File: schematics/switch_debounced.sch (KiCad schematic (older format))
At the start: 6 parts, among them SW1 SW_SPST

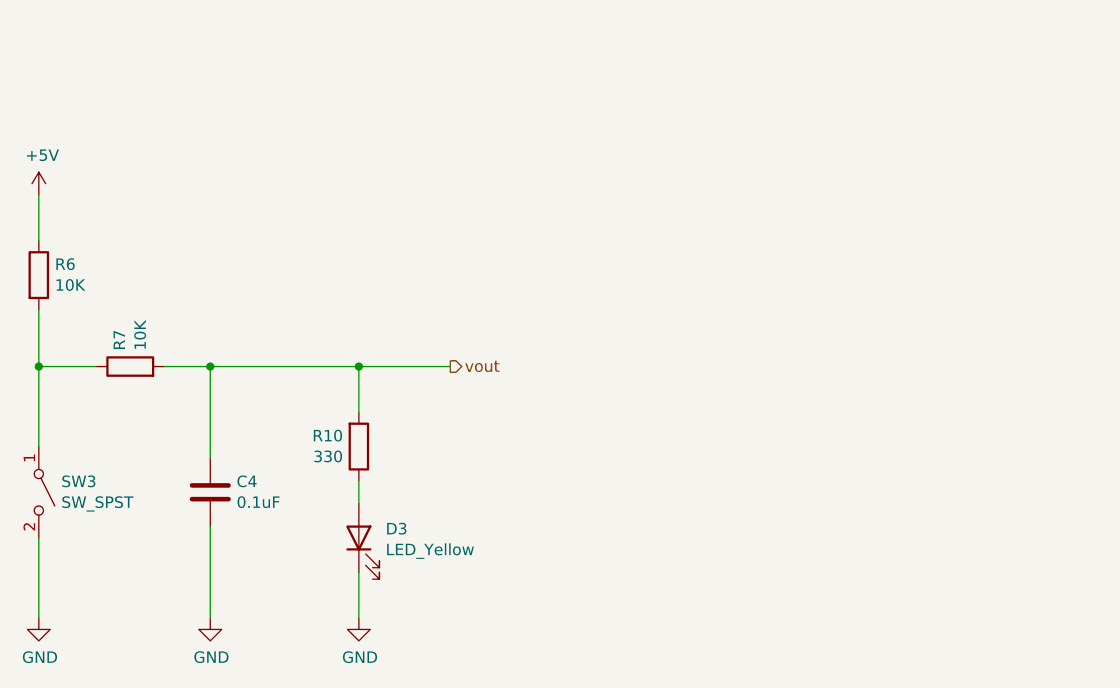
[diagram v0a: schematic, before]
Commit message: fixed lcd pin connections and xtra halls
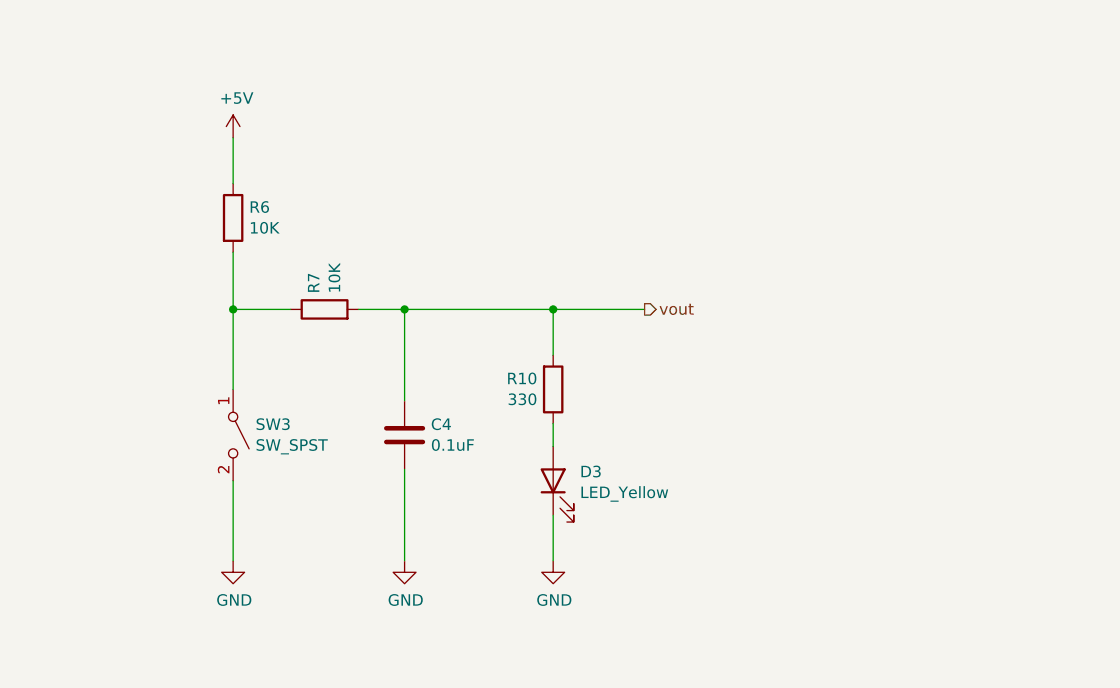
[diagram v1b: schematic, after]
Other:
- moved on the sheet: C4, D3, R10, R6, R7, SW3
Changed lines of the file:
@@
 EESchema Schematic File Version 4
-LIBS:odometer_project-cache
 EELAYER 30 0
 EELAYER END
 $Descr A4 11693 8268
 encoding utf-8
-Sheet 4 4
-Title ""
-Date ""
-Rev ""
-Comp ""
+Sheet 2 4
+Title "Odometer I2C Interface"
+Date "2020-10-03"
+Rev "2"
+Comp "DES Gang"
 Comment1 ""
 Comment2 ""
@@
 L Switch:SW_SPST SW1
 U 1 1 5F7A2F6B
-P 4050 4500
+P 4900 4250
 AR Path="/5F7B6E63/5F7A2F6B" Ref="SW1"  Part="1"
 AR Path="/5F7BFBA0/5F7A2F6B" Ref="SW2"  Part="1"
@@
 AR Path="/5F7CC063/5F7A2F6B" Ref="SW2"  Part="1"
 AR Path="/5F7CF7BD/5F7A2F6B" Ref="SW3"  Part="1"
-F 0 "SW3" V 4004 4598 50  0000 L CNN
-F 1 "SW_SPST" V 4095 4598 50  0000 L CNN
-F 2 "Button_Switch_THT:SW_PUSH_6mm_H4.3mm" H 4050 4500 50  0001 C CNN
-F 3 "~" H 4050 4500 50  0001 C CNN
-	1    4050 4500
+F 0 "SW3" V 4854 4348 50  0000 L CNN
+F 1 "SW_SPST" V 4945 4348 50  0000 L CNN
+F 2 "Button_Switch_THT:SW_PUSH_6mm_H4.3mm" H 4900 4250 50  0001 C CNN
+F 3 "~" H 4900 4250 50  0001 C CNN
+	1    4900 4250
 	0    1    1    0
 $EndComp
@@
 L power:GND #PWR0101
 U 1 1 5F7A3360
-P 4050 5050
+P 4900 4800
 AR Path="/5F7B6E63/5F7A3360" Ref="#PWR0101"  Part="1"
 AR Path="/5F7BFBA0/5F7A3360" Ref="#PWR0106"  Part="1"
@@
 AR Path="/5F7CC063/5F7A3360" Ref="#PWR0106"  Part="1"
 AR Path="/5F7CF7BD/5F7A3360" Ref="#PWR0113"  Part="1"
-F 0 "#PWR0113" H 4050 4800 50  0001 C CNN
-F 1 "GND" H 4055 4877 50  0000 C CNN
-F 2 "" H 4050 5050 50  0001 C CNN
-F 3 "" H 4050 5050 50  0001 C CNN
-	1    4050 5050
+F 0 "#PWR0113" H 4900 4550 50  0001 C CNN
+F 1 "GND" H 4905 4627 50  0000 C CNN
+F 2 "" H 4900 4800 50  0001 C CNN
+F 3 "" H 4900 4800 50  0001 C CNN
+	1    4900 4800
 	1    0    0    -1
 $EndComp
@@
 L power:+5V #PWR0102
 U 1 1 5F7A3875
-P 4050 3200
+P 4900 2950
 AR Path="/5F7B6E63/5F7A3875" Ref="#PWR0102"  Part="1"
 AR Path="/5F7BFBA0/5F7A3875" Ref="#PWR0107"  Part="1"
@@
 AR Path="/5F7CC063/5F7A3875" Ref="#PWR0107"  Part="1"
 AR Path="/5F7CF7BD/5F7A3875" Ref="#PWR0114"  Part="1"
-F 0 "#PWR0114" H 4050 3050 50  0001 C CNN
-F 1 "+5V" H 4065 3373 50  0000 C CNN
-F 2 "" H 4050 3200 50  0001 C CNN
-F 3 "" H 4050 3200 50  0001 C CNN
-	1    4050 3200
-	1    0    0    -1
-$EndComp
-Wire Wire Line
-	4050 3200 4050 3400
-Wire Wire Line
-	4050 4700 4050 5050
+F 0 "#PWR0114" H 4900 2800 50  0001 C CNN
+F 1 "+5V" H 4915 3123 50  0000 C CNN
+F 2 "" H 4900 2950 50  0001 C CNN
+F 3 "" H 4900 2950 50  0001 C CNN
+	1    4900 2950
+	1    0    0    -1
+$EndComp
+Wire Wire Line
+	4900 2950 4900 3150
+Wire Wire Line
+	4900 4450 4900 4800
 $Comp
 L Device:R R1
 U 1 1 5F7A4488
-P 4050 3550
+P 4900 3300
 AR Path="/5F7B6E63/5F7A4488" Ref="R1"  Part="1"
 AR Path="/5F7BFBA0/5F7A4488" Ref="R4"  Part="1"
@@
 AR Path="/5F7CC063/5F7A4488" Ref="R4"  Part="1"
 AR Path="/5F7CF7BD/5F7A4488" Ref="R6"  Part="1"
-F 0 "R6" H 4120 3596 50  0000 L CNN
-F 1 "10K" H 4120 3505 50  0000 L CNN
-F 2 "Resistor_SMD:R_0805_2012Metric_Pad1.15x1.40mm_HandSolder" V 3980 3550 50  0001 C CNN
-F 3 "~" H 4050 3550 50  0001 C CNN
-	1    4050 3550
-	1    0    0    -1
-$EndComp
-Wire Wire Line
-	4050 3700 4050 3950
-Wire Wire Line
-	4300 3950 4050 3950
-Connection ~ 4050 3950
-Wire Wire Line
-	4050 3950 4050 4300
+F 0 "R6" H 4970 3346 50  0000 L CNN
+F 1 "10K" H 4970 3255 50  0000 L CNN
+F 2 "Resistor_SMD:R_0805_2012Metric_Pad1.15x1.40mm_HandSolder" V 4830 3300 50  0001 C CNN
+F 3 "~" H 4900 3300 50  0001 C CNN
+	1    4900 3300
+	1    0    0    -1
+$EndComp
+Wire Wire Line
+	4900 3450 4900 3700
+Wire Wire Line
+	5150 3700 4900 3700
+Connection ~ 4900 3700
+Wire Wire Line
+	4900 3700 4900 4050
 $Comp
 L Device:C C2
 U 1 1 5F7A534F
-P 4800 4500
+P 5650 4250
 AR Path="/5F7B6E63/5F7A534F" Ref="C2"  Part="1"
 AR Path="/5F7BFBA0/5F7A534F" Ref="C3"  Part="1"
@@
 AR Path="/5F7CC063/5F7A534F" Ref="C3"  Part="1"
 AR Path="/5F7CF7BD/5F7A534F" Ref="C4"  Part="1"
-F 0 "C4" H 4915 4546 50  0000 L CNN
-F 1 "0.1uF" H 4915 4455 50  0000 L CNN
-F 2 "Capacitor_SMD:C_0805_2012Metric_Pad1.15x1.40mm_HandSolder" H 4838 4350 50  0001 C CNN
-F 3 "~" H 4800 4500 50  0001 C CNN
-	1    4800 4500
-	1    0    0    -1
-$EndComp
-Wire Wire Line
-	4800 4350 4800 3950
-Connection ~ 4800 3950
-Wire Wire Line
-	4800 3950 5450 3950
+F 0 "C4" H 5765 4296 50  0000 L CNN
+F 1 "0.1uF" H 5765 4205 50  0000 L CNN
+F 2 "Capacitor_SMD:C_0805_2012Metric_Pad1.15x1.40mm_HandSolder" H 5688 4100 50  0001 C CNN
+F 3 "~" H 5650 4250 50  0001 C CNN
+	1    5650 4250
+	1    0    0    -1
+$EndComp
+Wire Wire Line
+	5650 4100 5650 3700
+Connection ~ 5650 3700
+Wire Wire Line
+	5650 3700 6300 3700
 $Comp
 L power:GND #PWR0105
 U 1 1 5F7A59C8
-P 4800 5050
+P 5650 4800
 AR Path="/5F7B6E63/5F7A59C8" Ref="#PWR0105"  Part="1"
 AR Path="/5F7BFBA0/5F7A59C8" Ref="#PWR0112"  Part="1"
@@
 AR Path="/5F7CC063/5F7A59C8" Ref="#PWR0112"  Part="1"
 AR Path="/5F7CF7BD/5F7A59C8" Ref="#PWR0115"  Part="1"
-F 0 "#PWR0115" H 4800 4800 50  0001 C CNN
-F 1 "GND" H 4805 4877 50  0000 C CNN
-F 2 "" H 4800 5050 50  0001 C CNN
-F 3 "" H 4800 5050 50  0001 C CNN
-	1    4800 5050
-	1    0    0    -1
-$EndComp
-Wire Wire Line
-	4800 4650 4800 5050
-Text HLabel 5850 3950 2    50   Output ~ 0
+F 0 "#PWR0115" H 5650 4550 50  0001 C CNN
+F 1 "GND" H 5655 4627 50  0000 C CNN
+F 2 "" H 5650 4800 50  0001 C CNN
+F 3 "" H 5650 4800 50  0001 C CNN
+	1    5650 4800
+	1    0    0    -1
+$EndComp
+Wire Wire Line
+	5650 4400 5650 4800
+Text HLabel 6700 3700 2    50   Output ~ 0
 vout
 $Comp
 L Device:R R2
 U 1 1 5F7D50A7
-P 4450 3950
+P 5300 3700
 AR Path="/5F7B6E63/5F7D50A7" Ref="R2"  Part="1"
 AR Path="/5F7BFBA0/5F7D50A7" Ref="R?"  Part="1"
@@
 AR Path="/5F7CC063/5F7D50A7" Ref="R5"  Part="1"
 AR Path="/5F7CF7BD/5F7D50A7" Ref="R7"  Part="1"
-F 0 "R7" H 4520 3996 50  0000 L CNN
-F 1 "10K" H 4520 3905 50  0000 L CNN
-F 2 "Resistor_SMD:R_0805_2012Metric_Pad1.15x1.40mm_HandSolder" V 4380 3950 50  0001 C CNN
-F 3 "~" H 4450 3950 50  0001 C CNN
-	1    4450 3950
+F 0 "R7" H 5370 3746 50  0000 L CNN
+F 1 "10K" H 5370 3655 50  0000 L CNN
+F 2 "Resistor_SMD:R_0805_2012Metric_Pad1.15x1.40mm_HandSolder" V 5230 3700 50  0001 C CNN
+F 3 "~" H 5300 3700 50  0001 C CNN
+	1    5300 3700
 	0    -1   -1   0
 $EndComp
 Wire Wire Line
-	4600 3950 4800 3950
+	5450 3700 5650 3700
 $Comp
 L Device:LED D1
 U 1 1 5F8214CD
-P 5450 4700
+P 6300 4450
 AR Path="/5F7B6E63/5F8214CD" Ref="D1"  Part="1"
 AR Path="/5F7CC063/5F8214CD" Ref="D2"  Part="1"
 AR Path="/5F7CF7BD/5F8214CD" Ref="D3"  Part="1"
-F 0 "D3" V 5489 4583 50  0000 R CNN
-F 1 "LED_Yellow" V 5398 4583 50  0000 R CNN
-F 2 "LED_SMD:LED_0805_2012Metric_Pad1.15x1.40mm_HandSolder" H 5450 4700 50  0001 C CNN
-F 3 "~" H 5450 4700 50  0001 C CNN
-	1    5450 4700
+F 0 "D3" V 6339 4333 50  0000 R CNN
+F 1 "LED_Yellow" V 6248 4333 50  0000 R CNN
+F 2 "LED_SMD:LED_0805_2012Metric_Pad1.15x1.40mm_HandSolder" H 6300 4450 50  0001 C CNN
+F 3 "~" H 6300 4450 50  0001 C CNN
+	1    6300 4450
 	0    -1   -1   0
 $EndComp
 Wire Wire Line
-	5450 4450 5450 4550
+	6300 4200 6300 4300
 $Comp
 L Device:R R8
 U 1 1 5F8223FC
-P 5450 4300
+P 6300 4050
 AR Path="/5F7B6E63/5F8223FC" Ref="R8"  Part="1"
 AR Path="/5F7CC063/5F8223FC" Ref="R9"  Part="1"
 AR Path="/5F7CF7BD/5F8223FC" Ref="R10"  Part="1"
-F 0 "R10" H 5381 4254 50  0000 R CNN
-F 1 "330" H 5381 4345 50  0000 R CNN
-F 2 "Resistor_SMD:R_0805_2012Metric_Pad1.15x1.40mm_HandSolder" V 5380 4300 50  0001 C CNN
-F 3 "~" H 5450 4300 50  0001 C CNN
-	1    5450 4300
+F 0 "R10" H 6231 4004 50  0000 R CNN
+F 1 "330" H 6231 4095 50  0000 R CNN
+F 2 "Resistor_SMD:R_0805_2012Metric_Pad1.15x1.40mm_HandSolder" V 6230 4050 50  0001 C CNN
+F 3 "~" H 6300 4050 50  0001 C CNN
+	1    6300 4050
 	1    0    0    1
 $EndComp
 Wire Wire Line
-	5450 4150 5450 3950
-Connection ~ 5450 3950
-Wire Wire Line
-	5450 3950 5850 3950
+	6300 3900 6300 3700
+Connection ~ 6300 3700
+Wire Wire Line
+	6300 3700 6700 3700
 $Comp
 L power:GND #PWR03
 U 1 1 5F8242EB
-P 5450 5050
+P 6300 4800
 AR Path="/5F7B6E63/5F8242EB" Ref="#PWR03"  Part="1"
 AR Path="/5F7BFBA0/5F8242EB" Ref="#PWR?"  Part="1"
@@
 AR Path="/5F7CC063/5F8242EB" Ref="#PWR04"  Part="1"
 AR Path="/5F7CF7BD/5F8242EB" Ref="#PWR05"  Part="1"
-F 0 "#PWR05" H 5450 4800 50  0001 C CNN
-F 1 "GND" H 5455 4877 50  0000 C CNN
-F 2 "" H 5450 5050 50  0001 C CNN
-F 3 "" H 5450 5050 50  0001 C CNN
-	1    5450 5050
-	1    0    0    -1
-$EndComp
-Wire Wire Line
-	5450 4850 5450 5050
+F 0 "#PWR05" H 6300 4550 50  0001 C CNN
+F 1 "GND" H 6305 4627 50  0000 C CNN
+F 2 "" H 6300 4800 50  0001 C CNN
+F 3 "" H 6300 4800 50  0001 C CNN
+	1    6300 4800
+	1    0    0    -1
+$EndComp
+Wire Wire Line
+	6300 4600 6300 4800
 $EndSCHEMATC

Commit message: added schematic notes
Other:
- note added: "On our Proto Board Design, dont worry \nabout this circuit - just use a standard pull \ndown resistor with a switch and connect the \nrelevant lines to the relevant pins"
- moved on the sheet: C2, D1, R1, R2, R8, SW1
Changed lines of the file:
@@
 L Switch:SW_SPST SW1
 U 1 1 5F7A2F6B
-P 4900 4250
+P 4700 3950
 AR Path="/5F7B6E63/5F7A2F6B" Ref="SW1"  Part="1"
 AR Path="/5F7BFBA0/5F7A2F6B" Ref="SW2"  Part="1"
@@
 AR Path="/5F7CC063/5F7A2F6B" Ref="SW2"  Part="1"
 AR Path="/5F7CF7BD/5F7A2F6B" Ref="SW3"  Part="1"
-F 0 "SW3" V 4854 4348 50  0000 L CNN
-F 1 "SW_SPST" V 4945 4348 50  0000 L CNN
-F 2 "Button_Switch_THT:SW_PUSH_6mm_H4.3mm" H 4900 4250 50  0001 C CNN
-F 3 "~" H 4900 4250 50  0001 C CNN
-	1    4900 4250
+F 0 "SW1" V 4654 4048 50  0000 L CNN
+F 1 "SW_SPST" V 4745 4048 50  0000 L CNN
+F 2 "Button_Switch_THT:SW_PUSH_6mm_H4.3mm" H 4700 3950 50  0001 C CNN
+F 3 "~" H 4700 3950 50  0001 C CNN
+	1    4700 3950
 	0    1    1    0
 $EndComp
@@
 L power:GND #PWR0101
 U 1 1 5F7A3360
-P 4900 4800
+P 4700 4500
 AR Path="/5F7B6E63/5F7A3360" Ref="#PWR0101"  Part="1"
 AR Path="/5F7BFBA0/5F7A3360" Ref="#PWR0106"  Part="1"
@@
 AR Path="/5F7CC063/5F7A3360" Ref="#PWR0106"  Part="1"
 AR Path="/5F7CF7BD/5F7A3360" Ref="#PWR0113"  Part="1"
-F 0 "#PWR0113" H 4900 4550 50  0001 C CNN
-F 1 "GND" H 4905 4627 50  0000 C CNN
-F 2 "" H 4900 4800 50  0001 C CNN
-F 3 "" H 4900 4800 50  0001 C CNN
-	1    4900 4800
+F 0 "#PWR0101" H 4700 4250 50  0001 C CNN
+F 1 "GND" H 4705 4327 50  0000 C CNN
+F 2 "" H 4700 4500 50  0001 C CNN
+F 3 "" H 4700 4500 50  0001 C CNN
+	1    4700 4500
 	1    0    0    -1
 $EndComp
@@
 L power:+5V #PWR0102
 U 1 1 5F7A3875
-P 4900 2950
+P 4700 2650
 AR Path="/5F7B6E63/5F7A3875" Ref="#PWR0102"  Part="1"
 AR Path="/5F7BFBA0/5F7A3875" Ref="#PWR0107"  Part="1"
@@
 AR Path="/5F7CC063/5F7A3875" Ref="#PWR0107"  Part="1"
 AR Path="/5F7CF7BD/5F7A3875" Ref="#PWR0114"  Part="1"
-F 0 "#PWR0114" H 4900 2800 50  0001 C CNN
-F 1 "+5V" H 4915 3123 50  0000 C CNN
-F 2 "" H 4900 2950 50  0001 C CNN
-F 3 "" H 4900 2950 50  0001 C CNN
-	1    4900 2950
+F 0 "#PWR0102" H 4700 2500 50  0001 C CNN
+F 1 "+5V" H 4715 2823 50  0000 C CNN
+F 2 "" H 4700 2650 50  0001 C CNN
+F 3 "" H 4700 2650 50  0001 C CNN
+	1    4700 2650
 	1    0    0    -1
 $EndComp
 Wire Wire Line
-	4900 2950 4900 3150
+	4700 2650 4700 2850
 Wire Wire Line
-	4900 4450 4900 4800
+	4700 4150 4700 4500
 $Comp
 L Device:R R1
 U 1 1 5F7A4488
-P 4900 3300
+P 4700 3000
 AR Path="/5F7B6E63/5F7A4488" Ref="R1"  Part="1"
 AR Path="/5F7BFBA0/5F7A4488" Ref="R4"  Part="1"
@@
 AR Path="/5F7CC063/5F7A4488" Ref="R4"  Part="1"
 AR Path="/5F7CF7BD/5F7A4488" Ref="R6"  Part="1"
-F 0 "R6" H 4970 3346 50  0000 L CNN
-F 1 "10K" H 4970 3255 50  0000 L CNN
-F 2 "Resistor_SMD:R_0805_2012Metric_Pad1.15x1.40mm_HandSolder" V 4830 3300 50  0001 C CNN
-F 3 "~" H 4900 3300 50  0001 C CNN
-	1    4900 3300
+F 0 "R1" H 4770 3046 50  0000 L CNN
+F 1 "10K" H 4770 2955 50  0000 L CNN
+F 2 "Resistor_SMD:R_0805_2012Metric_Pad1.15x1.40mm_HandSolder" V 4630 3000 50  0001 C CNN
+F 3 "~" H 4700 3000 50  0001 C CNN
+	1    4700 3000
 	1    0    0    -1
 $EndComp
 Wire Wire Line
-	4900 3450 4900 3700
+	4700 3150 4700 3400
 Wire Wire Line
-	5150 3700 4900 3700
-Connection ~ 4900 3700
+	4950 3400 4700 3400
+Connection ~ 4700 3400
 Wire Wire Line
-	4900 3700 4900 4050
+	4700 3400 4700 3750
 $Comp
 L Device:C C2
 U 1 1 5F7A534F
-P 5650 4250
+P 5450 3950
 AR Path="/5F7B6E63/5F7A534F" Ref="C2"  Part="1"
 AR Path="/5F7BFBA0/5F7A534F" Ref="C3"  Part="1"
@@
 AR Path="/5F7CC063/5F7A534F" Ref="C3"  Part="1"
 AR Path="/5F7CF7BD/5F7A534F" Ref="C4"  Part="1"
-F 0 "C4" H 5765 4296 50  0000 L CNN
-F 1 "0.1uF" H 5765 4205 50  0000 L CNN
-F 2 "Capacitor_SMD:C_0805_2012Metric_Pad1.15x1.40mm_HandSolder" H 5688 4100 50  0001 C CNN
-F 3 "~" H 5650 4250 50  0001 C CNN
-	1    5650 4250
+F 0 "C2" H 5565 3996 50  0000 L CNN
+F 1 "0.1uF" H 5565 3905 50  0000 L CNN
+F 2 "Capacitor_SMD:C_0805_2012Metric_Pad1.15x1.40mm_HandSolder" H 5488 3800 50  0001 C CNN
+F 3 "~" H 5450 3950 50  0001 C CNN
+	1    5450 3950
 	1    0    0    -1
 $EndComp
 Wire Wire Line
-	5650 4100 5650 3700
-Connection ~ 5650 3700
+	5450 3800 5450 3400
+Connection ~ 5450 3400
 Wire Wire Line
-	5650 3700 6300 3700
+	5450 3400 6100 3400
 $Comp
 L power:GND #PWR0105
 U 1 1 5F7A59C8
-P 5650 4800
+P 5450 4500
 AR Path="/5F7B6E63/5F7A59C8" Ref="#PWR0105"  Part="1"
 AR Path="/5F7BFBA0/5F7A59C8" Ref="#PWR0112"  Part="1"
@@
 AR Path="/5F7CC063/5F7A59C8" Ref="#PWR0112"  Part="1"
 AR Path="/5F7CF7BD/5F7A59C8" Ref="#PWR0115"  Part="1"
-F 0 "#PWR0115" H 5650 4550 50  0001 C CNN
-F 1 "GND" H 5655 4627 50  0000 C CNN
-F 2 "" H 5650 4800 50  0001 C CNN
-F 3 "" H 5650 4800 50  0001 C CNN
-	1    5650 4800
+F 0 "#PWR0105" H 5450 4250 50  0001 C CNN
+F 1 "GND" H 5455 4327 50  0000 C CNN
+F 2 "" H 5450 4500 50  0001 C CNN
+F 3 "" H 5450 4500 50  0001 C CNN
+	1    5450 4500
 	1    0    0    -1
 $EndComp
 Wire Wire Line
-	5650 4400 5650 4800
-Text HLabel 6700 3700 2    50   Output ~ 0
+	5450 4100 5450 4500
+Text HLabel 6500 3400 2    50   Output ~ 0
 vout
 $Comp
 L Device:R R2
 U 1 1 5F7D50A7
-P 5300 3700
+P 5100 3400
 AR Path="/5F7B6E63/5F7D50A7" Ref="R2"  Part="1"
 AR Path="/5F7BFBA0/5F7D50A7" Ref="R?"  Part="1"
@@
 AR Path="/5F7CC063/5F7D50A7" Ref="R5"  Part="1"
 AR Path="/5F7CF7BD/5F7D50A7" Ref="R7"  Part="1"
-F 0 "R7" H 5370 3746 50  0000 L CNN
-F 1 "10K" H 5370 3655 50  0000 L CNN
-F 2 "Resistor_SMD:R_0805_2012Metric_Pad1.15x1.40mm_HandSolder" V 5230 3700 50  0001 C CNN
-F 3 "~" H 5300 3700 50  0001 C CNN
-	1    5300 3700
+F 0 "R2" H 5170 3446 50  0000 L CNN
+F 1 "10K" H 5170 3355 50  0000 L CNN
+F 2 "Resistor_SMD:R_0805_2012Metric_Pad1.15x1.40mm_HandSolder" V 5030 3400 50  0001 C CNN
+F 3 "~" H 5100 3400 50  0001 C CNN
+	1    5100 3400
 	0    -1   -1   0
 $EndComp
 Wire Wire Line
-	5450 3700 5650 3700
+	5250 3400 5450 3400
 $Comp
 L Device:LED D1
 U 1 1 5F8214CD
-P 6300 4450
+P 6100 4150
 AR Path="/5F7B6E63/5F8214CD" Ref="D1"  Part="1"
 AR Path="/5F7CC063/5F8214CD" Ref="D2"  Part="1"
 AR Path="/5F7CF7BD/5F8214CD" Ref="D3"  Part="1"
-F 0 "D3" V 6339 4333 50  0000 R CNN
-F 1 "LED_Yellow" V 6248 4333 50  0000 R CNN
-F 2 "LED_SMD:LED_0805_2012Metric_Pad1.15x1.40mm_HandSolder" H 6300 4450 50  0001 C CNN
-F 3 "~" H 6300 4450 50  0001 C CNN
-	1    6300 4450
+F 0 "D1" V 6139 4033 50  0000 R CNN
+F 1 "LED_Yellow" V 6048 4033 50  0000 R CNN
+F 2 "LED_SMD:LED_0805_2012Metric_Pad1.15x1.40mm_HandSolder" H 6100 4150 50  0001 C CNN
+F 3 "~" H 6100 4150 50  0001 C CNN
+	1    6100 4150
 	0    -1   -1   0
 $EndComp
 Wire Wire Line
-	6300 4200 6300 4300
+	6100 3900 6100 4000
 $Comp
 L Device:R R8
 U 1 1 5F8223FC
-P 6300 4050
+P 6100 3750
 AR Path="/5F7B6E63/5F8223FC" Ref="R8"  Part="1"
 AR Path="/5F7CC063/5F8223FC" Ref="R9"  Part="1"
 AR Path="/5F7CF7BD/5F8223FC" Ref="R10"  Part="1"
-F 0 "R10" H 6231 4004 50  0000 R CNN
-F 1 "330" H 6231 4095 50  0000 R CNN
-F 2 "Resistor_SMD:R_0805_2012Metric_Pad1.15x1.40mm_HandSolder" V 6230 4050 50  0001 C CNN
-F 3 "~" H 6300 4050 50  0001 C CNN
-	1    6300 4050
+F 0 "R8" H 6031 3704 50  0000 R CNN
+F 1 "330" H 6031 3795 50  0000 R CNN
+F 2 "Resistor_SMD:R_0805_2012Metric_Pad1.15x1.40mm_HandSolder" V 6030 3750 50  0001 C CNN
+F 3 "~" H 6100 3750 50  0001 C CNN
+	1    6100 3750
 	1    0    0    1
 $EndComp
 Wire Wire Line
-	6300 3900 6300 3700
-Connection ~ 6300 3700
+	6100 3600 6100 3400
+Connection ~ 6100 3400
 Wire Wire Line
-	6300 3700 6700 3700
+	6100 3400 6500 3400
 $Comp
 L power:GND #PWR03
 U 1 1 5F8242EB
-P 6300 4800
+P 6100 4500
 AR Path="/5F7B6E63/5F8242EB" Ref="#PWR03"  Part="1"
 AR Path="/5F7BFBA0/5F8242EB" Ref="#PWR?"  Part="1"
@@
 AR Path="/5F7CC063/5F8242EB" Ref="#PWR04"  Part="1"
 AR Path="/5F7CF7BD/5F8242EB" Ref="#PWR05"  Part="1"
-F 0 "#PWR05" H 6300 4550 50  0001 C CNN
-F 1 "GND" H 6305 4627 50  0000 C CNN
-F 2 "" H 6300 4800 50  0001 C CNN
-F 3 "" H 6300 4800 50  0001 C CNN
-	1    6300 4800
+F 0 "#PWR03" H 6100 4250 50  0001 C CNN
+F 1 "GND" H 6105 4327 50  0000 C CNN
+F 2 "" H 6100 4500 50  0001 C CNN
+F 3 "" H 6100 4500 50  0001 C CNN
+	1    6100 4500
 	1    0    0    -1
 $EndComp
 Wire Wire Line
-	6300 4600 6300 4800
+	6100 4300 6100 4500
+Text Notes 6550 3950 0    50   ~ 10
+On our Proto Board Design, dont worry \nabout this circuit - just use a standard pull \ndown resistor with a switch and connect the \nrelevant lines to the relevant pins
 $EndSCHEMATC
